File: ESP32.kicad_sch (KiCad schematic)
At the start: 0 parts

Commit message: Test branching 1
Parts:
- added U1: CP2102N-Axx-xQFN28, Package_DFN_QFN:QFN-28-1EP_5x5mm_P0.5mm_EP3.35x3.35mm, symbol Interface_USB:CP2102N-Axx-xQFN28
- added U4: ESP32-WROOM-32, RF_Module:ESP32-WROOM-32, symbol RF_Module:ESP32-WROOM-32
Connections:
- new net: U1.29 (GND), U1.3 (GND)
- new net: U4.1 (GND), U4.15 (GND), U4.38 (GND), U4.39 (GND)
- new net Boot: U4.25 (IO0)
- new net LED_2: U4.29 (IO5)
- new net MOTOR_1: U4.26 (IO4)
- new net RX: U4.34 (RXD0/IO3)
- new net RXD2: U4.27 (IO16)
- new net SRV1: U4.14 (IO12)
- new net SRV2: U4.13 (IO14)
- new net TX: U4.35 (TXD0/IO1)
- new net TXD2: U4.28 (IO17)
- new net USB_DN: U1.5 (D-)
- new net USB_DP: U1.4 (D+)
- no-connect marks 0 -> 3
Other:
- note added: "CP2102 USB to UART Bridge [For ESP32 USB Communication]"

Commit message: Commit ESP 50%
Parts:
- added C1: C, symbol Device:C
- renumbered U1 to U?, U4 to U?
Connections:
- net GND: now reaches U?.1 (GND), U?.15 (GND), U?.38 (GND), U?.39 (GND)
- net GND: now also C1.2
- net MOTOR_4: now reaches U?.10 (IO25)
- net SRV4: now reaches U?.11 (IO26)
- net SRV3: now reaches U?.12 (IO27)
- net EN: now reaches U?.3 (EN)
- net EN: now also C1.1
- net LED_3: now reaches U?.30 (IO18)
- net SDA: now reaches U?.33 (IO21)
- net SCL: now reaches U?.36 (IO22)
- net LED_1: now reaches U?.37 (IO23)
- net BATT_Vdc: now reaches U?.7 (IO35)
- net MOTOR_3: now reaches U?.8 (IO32)
- net MOTOR_2: now reaches U?.9 (IO33)
- no-connect marks 3 -> 11

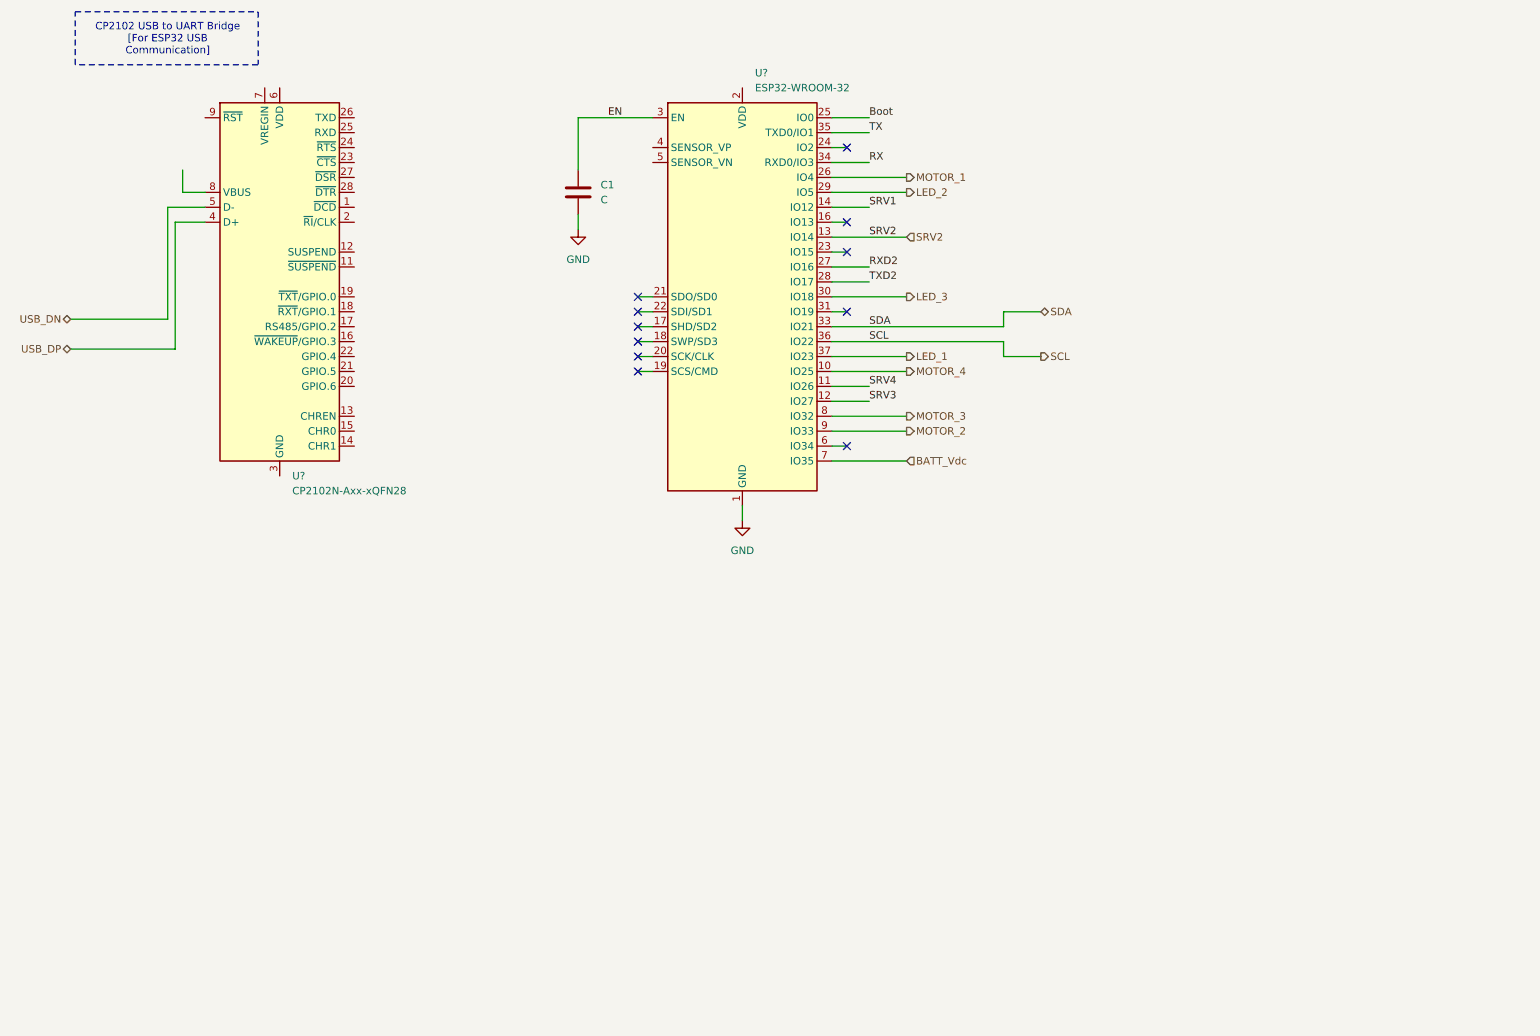
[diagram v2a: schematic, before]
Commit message: ESP finished symbol assembly
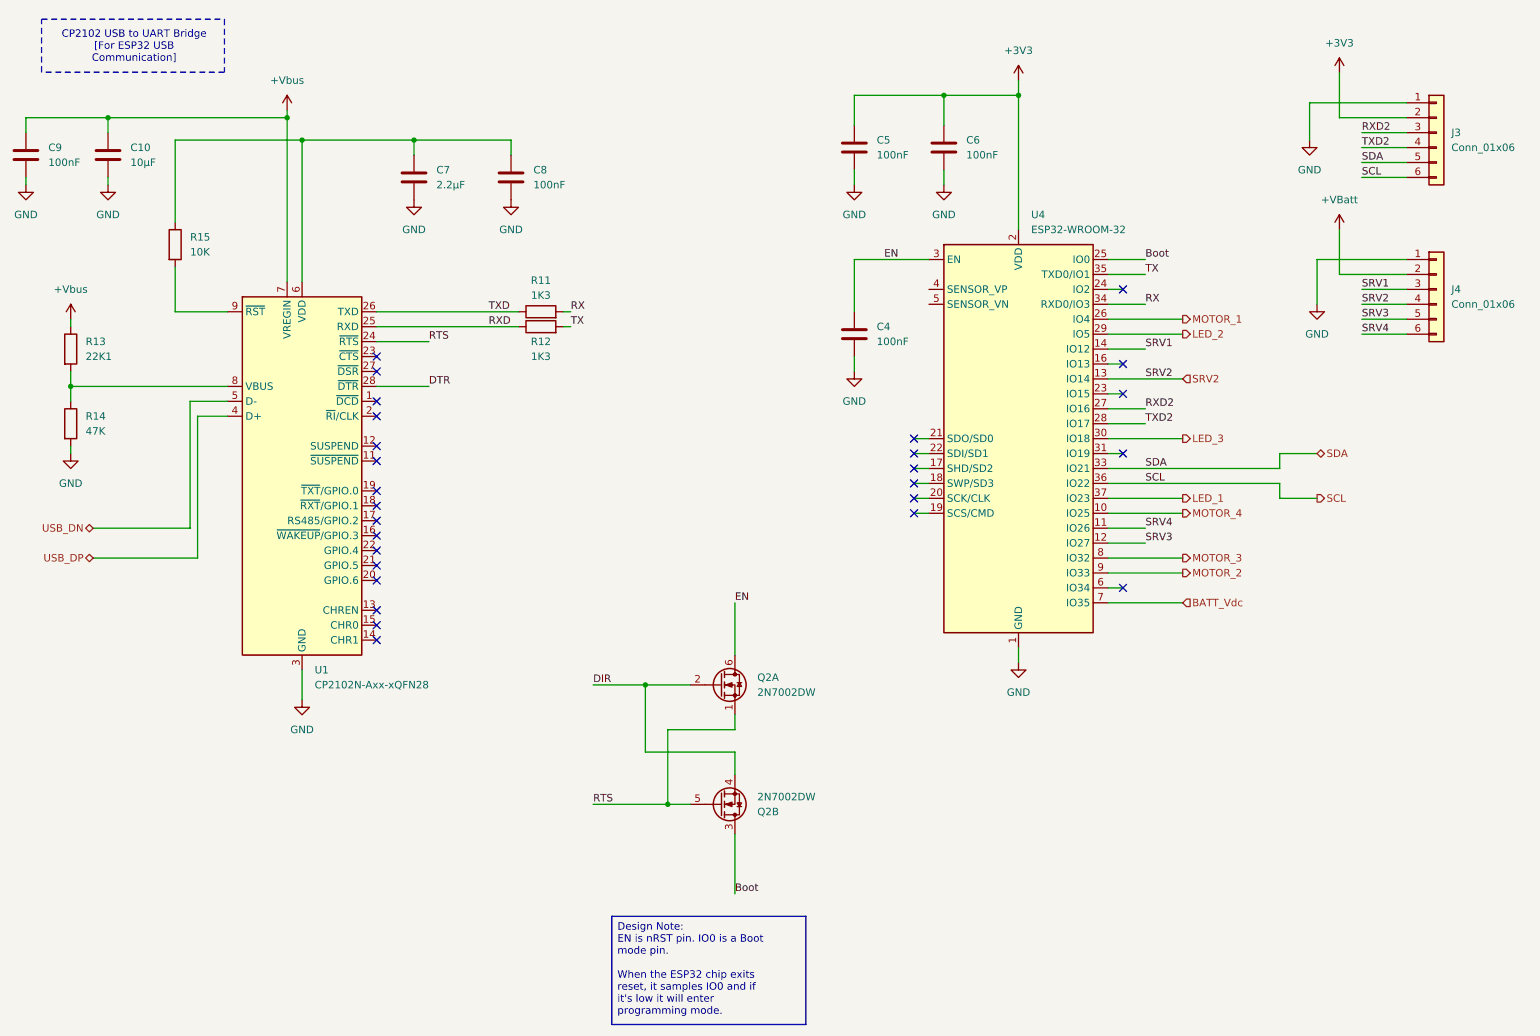
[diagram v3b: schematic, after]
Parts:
- removed C1: C, symbol Device:C
- added C10: 10μF, Capacitor_SMD:C_0603_1608Metric, symbol AI_CAPACITORS:C
- added C4, C5, C6, C8, C9: 100nF, Capacitor_SMD:C_0603_1608Metric, symbol AI_CAPACITORS:C
- added C7: 2.2μF, Capacitor_SMD:C_0603_1608Metric, symbol AI_CAPACITORS:C
- added J3, J4: Conn_01x06, Connector_PinHeader_2.54mm:PinHeader_1x06_P2.54mm_Vertical, symbol AI_CONNECTORS:Conn_01x06
- added Q2: 2N7002DW, symbol Transistor_FET:Q_Dual_NMOS_S1G1D2S2G2D1
- added R11, R12: 1K3, symbol Device:R
- added R13: 22K1, Resistor_SMD:R_0603_1608Metric, symbol AI_RESISTORS:R
- added R14: 47K, Resistor_SMD:R_0603_1608Metric, symbol AI_RESISTORS:R
- added R15: 10K, Resistor_SMD:R_0603_1608Metric, symbol AI_RESISTORS:R
- gave numbers to parts that had none: 2
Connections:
- net Boot: now also Q2.3 (D)
- net EN: now also C4.1, Q2.6 (D)
- net GND: now also U1.29 (GND), U1.3 (GND), C10.2, C4.2, C5.2, C6.2, C7.2, C8.2, C9.2, J3.1 (Pin_1), J4.1 (Pin_1), R14.2
- net RX: now also R11.2
- net RXD2: now also J3.3 (Pin_3)
- net SCL: now also J3.6 (Pin_6)
- net SDA: now also J3.5 (Pin_5)
- net SRV1: now also J4.3 (Pin_3)
- net SRV2: now also J4.4 (Pin_4)
- net SRV3: now also J4.5 (Pin_5)
- net SRV4: now also J4.6 (Pin_6)
- net TX: now also R12.2
- net TXD2: now also J3.4 (Pin_4)
- net RTS: now reaches U1.24 (~{RTS})
- net RTS: now also Q2.1 (S), Q2.5 (G)
- net RXD: now reaches U1.25 (RXD)
- net RXD: now also R12.1
- net TXD: now reaches U1.26 (TXD)
- net TXD: now also R11.1
- net DTR: now reaches U1.28 (~{DTR})
- net at U1.6 (VDD): now also C7.1, C8.1, R15.1
- net +Vbus: now reaches U1.7 (VREGIN)
- net +Vbus: now also C10.1, C9.1, R13.1
- net at U1.8 (VBUS): now also R13.2, R14.1
- net at U1.9 (~{RST}): now also R15.2
- net +3V3: now reaches U4.2 (VDD)
- net +3V3: now also C5.1, C6.1, J3.2 (Pin_2)
- new net +VBatt: J4.2 (Pin_2)
- new net DIR: Q2.2 (G), Q2.4 (S)
- no-connect marks 11 -> 27
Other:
- moved on the sheet: U1, U4

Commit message: All component assembly ready. Pending net classifications
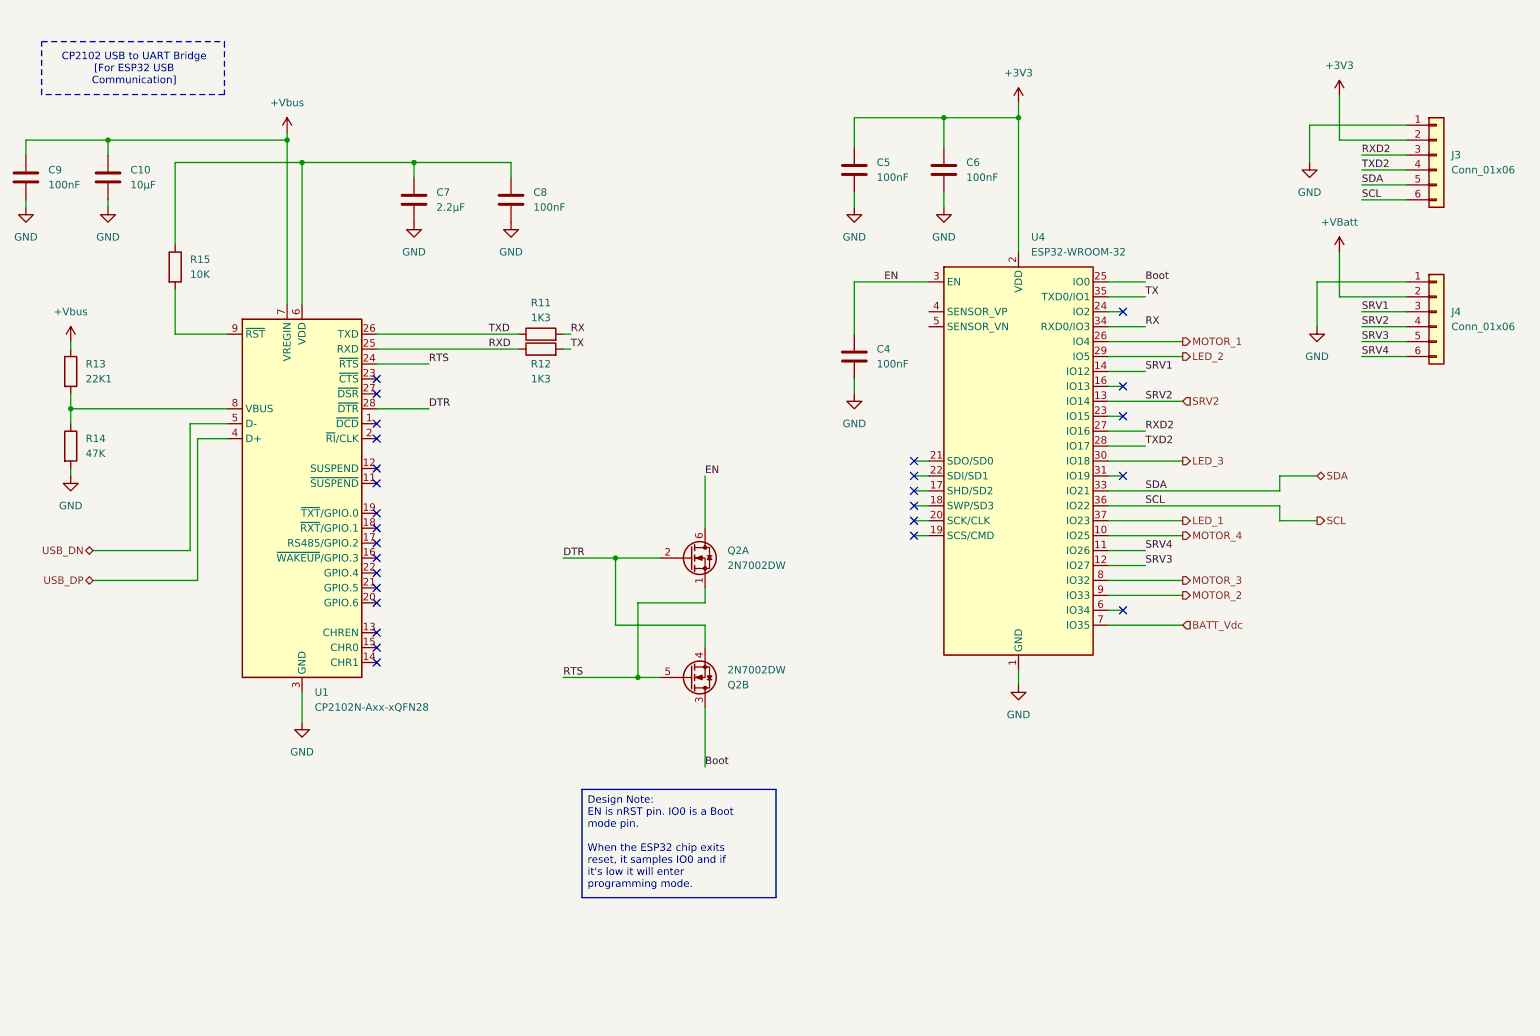
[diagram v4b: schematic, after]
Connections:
- net DIR is gone; now on net DTR: Q2.2 (G), Q2.4 (S)
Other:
- moved on the sheet: C10, C4, C5, C6, C7, C8, C9, J3, J4, Q2A, Q2B, R11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
